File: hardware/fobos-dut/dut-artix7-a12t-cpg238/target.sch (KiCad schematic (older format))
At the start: 37 parts, among them J1 Target, J10 Barrel_Jack_Switch, J2 Pmod 2x6, U2 SP3003-04ATG, U3 SP3003-04ATG, U4 SP3003-04ATG, U7 TS3A5018DBQR

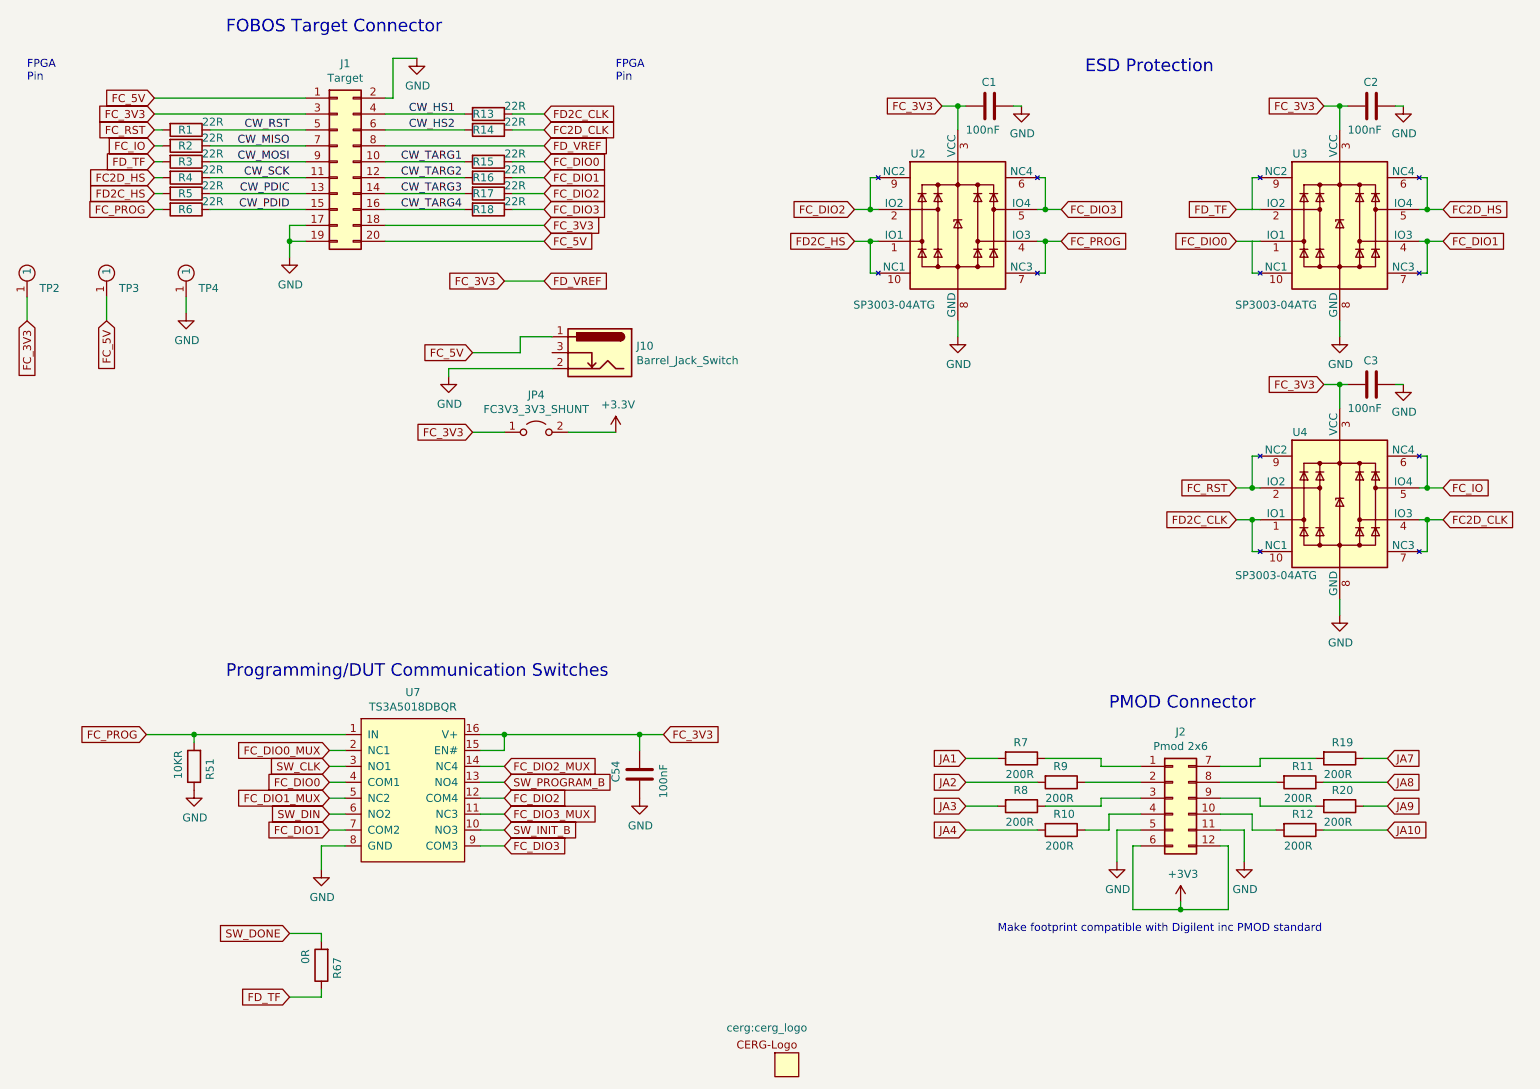
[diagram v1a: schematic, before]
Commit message: updated library ref for diode and FET, placed target connector and some parts
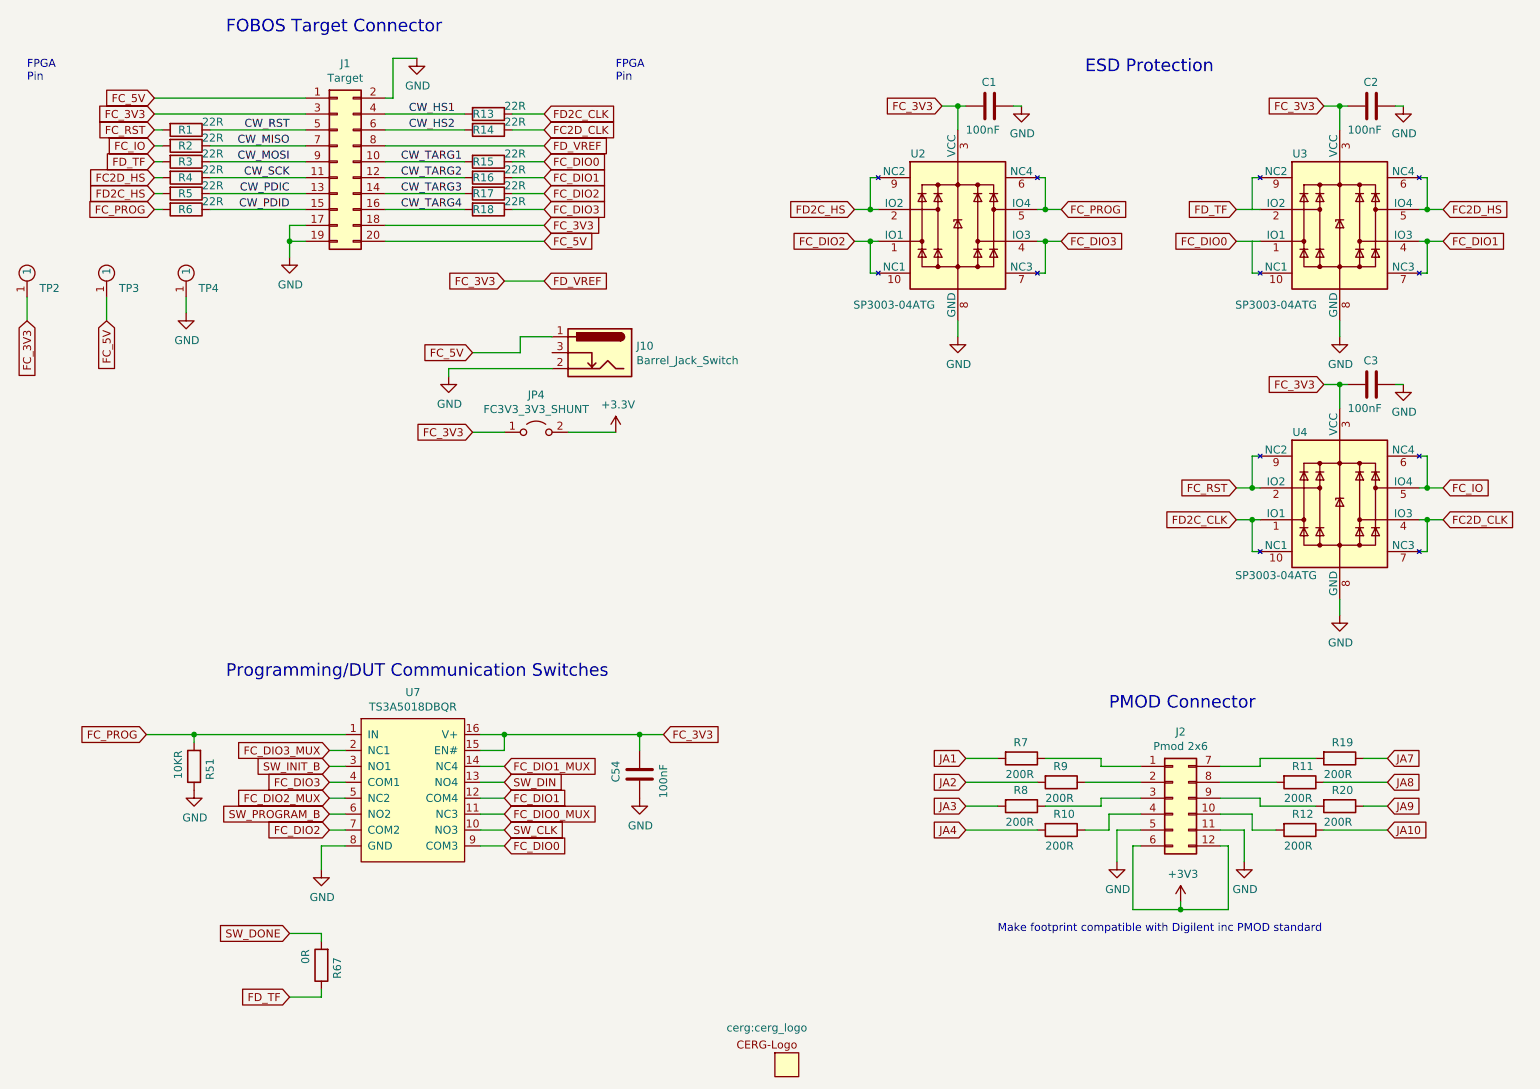
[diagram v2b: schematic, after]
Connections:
- net FC_DIO0: now also U7.9 (COM3); no longer U7.4 (COM1)
- net FC_DIO0_MUX: now also U7.11 (NC3); no longer U7.2 (NC1)
- net FC_DIO1: now also U7.12 (COM4); no longer U7.7 (COM2)
- net FC_DIO1_MUX: now also U7.14 (NC4); no longer U7.5 (NC2)
- net FC_DIO2: now also U2.1 (IO1), U2.10 (NC1), U7.7 (COM2); no longer U2.2 (IO2), U2.9 (NC2), U7.12 (COM4)
- net FC_DIO2_MUX: now also U7.5 (NC2); no longer U7.14 (NC4)
- net FC_DIO3: now also U2.4 (IO3), U2.7 (NC3), U7.4 (COM1); no longer U2.5 (IO4), U2.6 (NC4), U7.9 (COM3)
- net FC_DIO3_MUX: now also U7.2 (NC1); no longer U7.11 (NC3)
- net FC_PROG: now also U2.5 (IO4), U2.6 (NC4); no longer U2.4 (IO3), U2.7 (NC3)
- net FD2C_HS: now also U2.2 (IO2), U2.9 (NC2); no longer U2.1 (IO1), U2.10 (NC1)
- net SW_CLK: now also U7.10 (NO3); no longer U7.3 (NO1)
- net SW_DIN: now also U7.13 (NO4); no longer U7.6 (NO2)
- net SW_INIT_B: now also U7.3 (NO1); no longer U7.10 (NO3)
- net SW_PROGRAM_B: now also U7.6 (NO2); no longer U7.13 (NO4)
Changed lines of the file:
@@
 Wire Wire Line
 	4000 2400 4250 2400
-Text GLabel 7500 2150 2    50   Input ~ 0
+Text GLabel 7500 1950 2    50   Input ~ 0
 FC_PROG
 Text GLabel 8600 3900 0    50   Input ~ 0
 FD2C_CLK
-Text GLabel 6200 2150 0    50   Input ~ 0
+Text GLabel 6200 1950 0    50   Input ~ 0
 FD2C_HS
 Wire Wire Line
@@
 Wire Wire Line
 	6300 1950 6300 1750
-Text GLabel 7500 1950 2    50   Input ~ 0
+Text GLabel 7500 2150 2    50   Input ~ 0
 FC_DIO3
 Wire Wire Line
@@
 Text GLabel 6750 1300 0    50   Input ~ 0
 FC_3V3
-Text GLabel 6200 1950 0    50   Input ~ 0
+Text GLabel 6200 2150 0    50   Input ~ 0
 FC_DIO2
 $Comp
@@
 	1    0    0    -1
 $EndComp
+Text GLabel 4000 5850 2    50   Input ~ 0
+SW_CLK
+Text GLabel 4000 5750 2    50   Input ~ 0
+FC_DIO0_MUX
+Text GLabel 4000 5950 2    50   Input ~ 0
+FC_DIO0
+Text GLabel 4000 5550 2    50   Input ~ 0
+SW_DIN
+Text GLabel 4000 5450 2    50   Input ~ 0
+FC_DIO1_MUX
+Text GLabel 4000 5650 2    50   Input ~ 0
+FC_DIO1
+Text GLabel 2900 5550 0    50   Input ~ 0
+FC_DIO3
+Text GLabel 2900 5350 0    50   Input ~ 0
+FC_DIO3_MUX
 Text GLabel 2900 5450 0    50   Input ~ 0
-SW_CLK
-Text GLabel 2900 5350 0    50   Input ~ 0
-FC_DIO0_MUX
-Text GLabel 2900 5550 0    50   Input ~ 0
-FC_DIO0
+SW_INIT_B
+Text GLabel 2900 5850 0    50   Input ~ 0
+FC_DIO2
+Text GLabel 2900 5650 0    50   Input ~ 0
+FC_DIO2_MUX
 Text GLabel 2900 5750 0    50   Input ~ 0
-SW_DIN
-Text GLabel 2900 5650 0    50   Input ~ 0
-FC_DIO1_MUX
-Text GLabel 2900 5850 0    50   Input ~ 0
-FC_DIO1
-Text GLabel 4000 5950 2    50   Input ~ 0
-FC_DIO3
-Text GLabel 4000 5750 2    50   Input ~ 0
-FC_DIO3_MUX
-Text GLabel 4000 5850 2    50   Input ~ 0
-SW_INIT_B
-Text GLabel 4000 5650 2    50   Input ~ 0
-FC_DIO2
-Text GLabel 4000 5450 2    50   Input ~ 0
-FC_DIO2_MUX
-Text GLabel 4000 5550 2    50   Input ~ 0
 SW_PROGRAM_B
 Wire Wire Line

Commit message: fixed PMOD
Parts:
- J2: footprint Connector_PinHeader_2.54mm:PinHeader_2x06_P2.54mm_Horizontal -> fobos-shield:PinSocket_2x06_P2.54mm_Horizontal_FLipped
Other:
- note removed: "Make footprint compatible with Digilent inc PMOD standard"
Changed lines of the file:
@@
 F 0 "J2" H 8250 6067 50  0000 C CNN
 F 1 "Pmod 2x6" H 8250 5976 50  0000 C CNN
-F 2 "Connector_PinHeader_2.54mm:PinHeader_2x06_P2.54mm_Horizontal" H 8200 5650 50  0001 C CNN
+F 2 "fobos-shield:PinSocket_2x06_P2.54mm_Horizontal_FLipped" H 8200 5650 50  0001 C CNN
 F 3 "~" H 8200 5650 50  0001 C CNN
 F 4 "CONN HEADER R/A 12POS 2.54MM" H 8200 5650 50  0001 C CNN "Description"
@@
 	1    0    0    -1
 $EndComp
-Text Notes 7100 6500 0    50   ~ 0
-Make footprint compatible with Digilent inc PMOD standard
 $Comp
 L power:+3V3 #PWR?

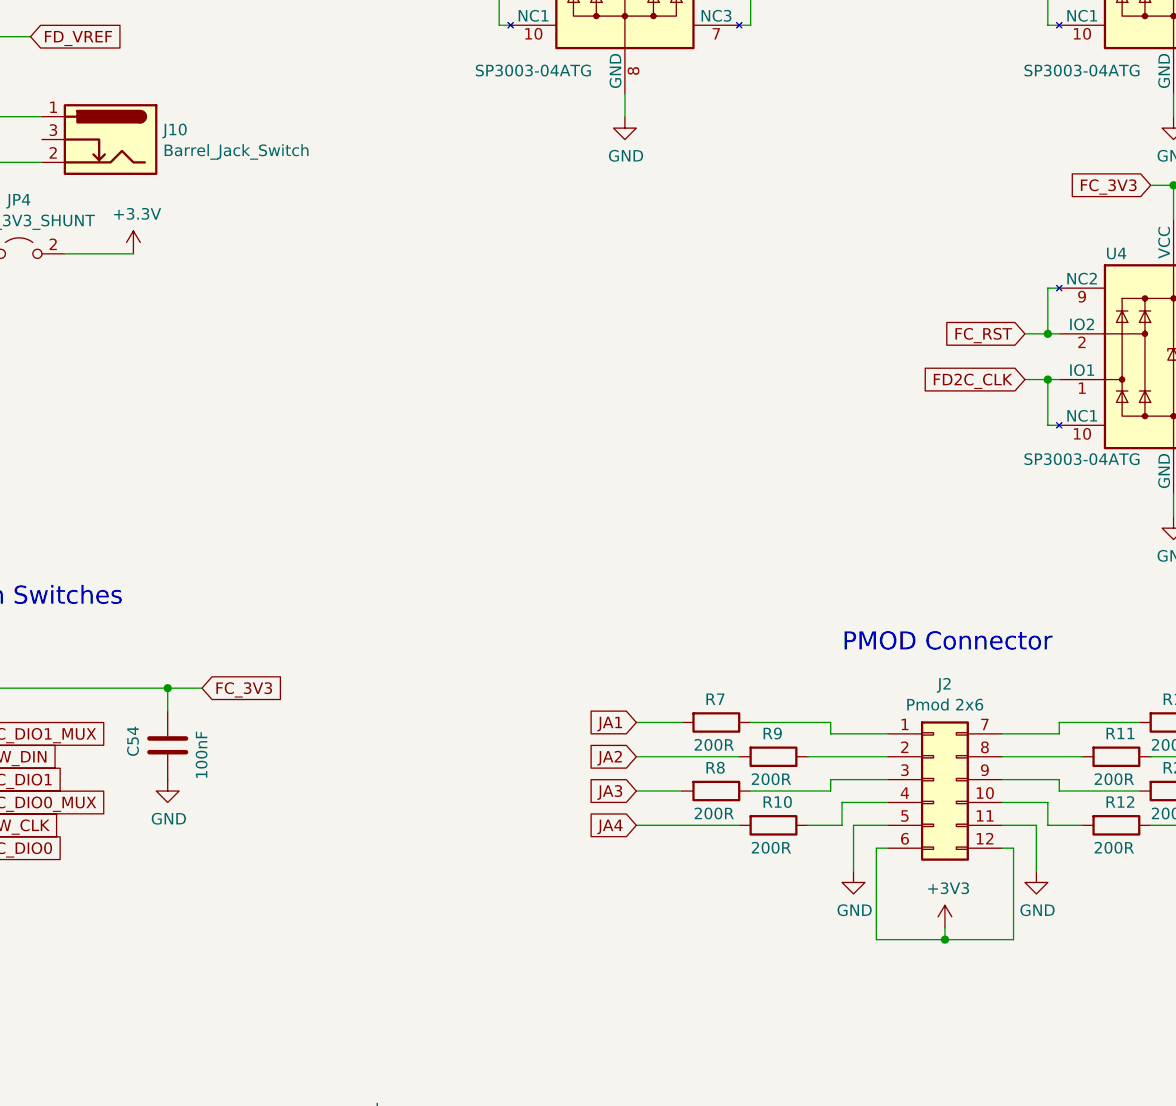
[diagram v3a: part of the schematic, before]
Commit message: added protection for PMOD
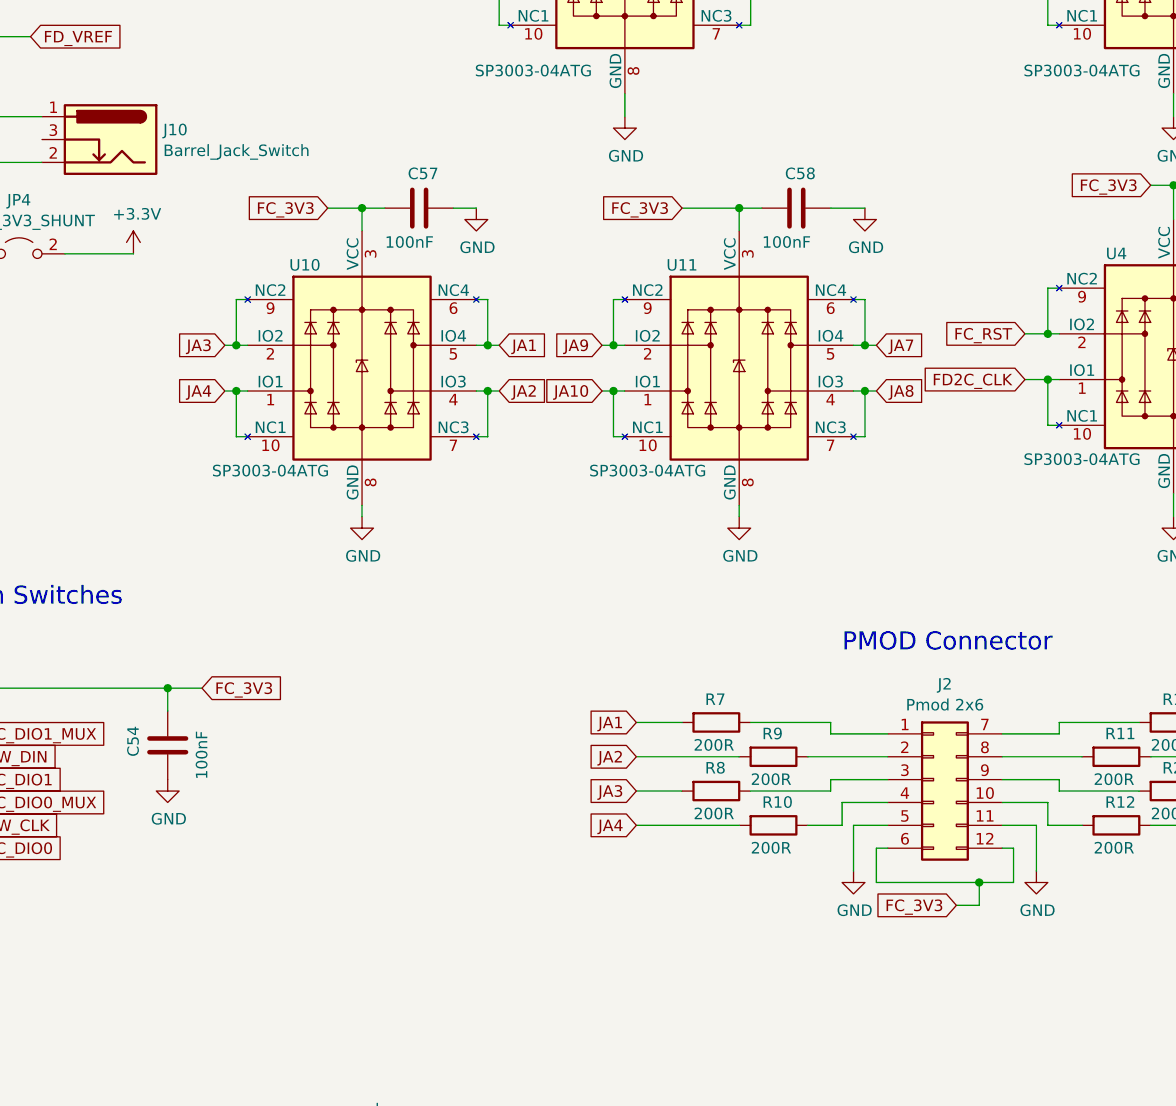
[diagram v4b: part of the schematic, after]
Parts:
- added C57, C58: 100nF, Capacitor_SMD:C_0603_1608Metric, symbol Device:C
- added U10, U11: SP3003-04ATG, Package_SO:MSOP-10_3x3mm_P0.5mm, symbol cerg:SP3003-04ATG
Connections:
- net +3V3: no longer J2.12 (Pin_12), J2.6 (Pin_6)
- net FC_3V3: now also J2.12 (Pin_12), J2.6 (Pin_6), C57.2, C58.2, U10.3 (VCC), U11.3 (VCC)
- net GND: now also C57.1, C58.1, U10.8 (GND), U11.8 (GND)
- net JA1: now also U10.5 (IO4), U10.6 (NC4)
- net JA10: now also U11.1 (IO1), U11.10 (NC1)
- net JA2: now also U10.4 (IO3), U10.7 (NC3)
- net JA3: now also U10.2 (IO2), U10.9 (NC2)
- net JA4: now also U10.1 (IO1), U10.10 (NC1)
- net JA7: now also U11.5 (IO4), U11.6 (NC4)
- net JA8: now also U11.4 (IO3), U11.7 (NC3)
- net JA9: now also U11.2 (IO2), U11.9 (NC2)

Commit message: everything placed on top except decoupling caps
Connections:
- net JA2: now also U10.2 (IO2), U10.9 (NC2); no longer U10.4 (IO3), U10.7 (NC3)
- net JA3: now also U11.5 (IO4), U11.6 (NC4); no longer U10.2 (IO2), U10.9 (NC2)
- net JA4: now also U11.2 (IO2), U11.9 (NC2); no longer U10.1 (IO1), U10.10 (NC1)
- net JA7: now also U10.4 (IO3), U10.7 (NC3); no longer U11.5 (IO4), U11.6 (NC4)
- net JA8: now also U10.1 (IO1), U10.10 (NC1); no longer U11.4 (IO3), U11.7 (NC3)
- net JA9: now also U11.4 (IO3), U11.7 (NC3); no longer U11.2 (IO2), U11.9 (NC2)
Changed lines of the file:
@@
 Text GLabel 6300 3750 2    50   Input ~ 0
 JA1
-Text GLabel 6300 3950 2    50   Input ~ 0
+Text GLabel 5100 3750 0    50   Input ~ 0
 JA2
-Text GLabel 5100 3750 0    50   Input ~ 0
+Text GLabel 7950 3750 2    50   Input ~ 0
 JA3
-Text GLabel 5100 3950 0    50   Input ~ 0
+Text GLabel 6750 3750 0    50   Input ~ 0
 JA4
 $Comp
@@
 	1    0    0    -1
 $EndComp
-Text GLabel 7950 3750 2    50   Input ~ 0
+Text GLabel 6300 3950 2    50   Input ~ 0
 JA7
+Text GLabel 5100 3950 0    50   Input ~ 0
+JA8
 Text GLabel 7950 3950 2    50   Input ~ 0
-JA8
-Text GLabel 6750 3750 0    50   Input ~ 0
 JA9
 Text GLabel 6750 3950 0    50   Input ~ 0

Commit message: almost last review
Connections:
- net FC_3V3: no longer U7.15 (EN#)
- net GND: now also U7.15 (EN#)
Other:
- moved on the sheet: C54
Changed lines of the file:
@@
 Comment1 "License: Apache License Version 2.0"
 Comment2 "Copyright © Cryptographic Engineering Research Group"
-Comment3 "Author: Jens-Peter Kaps"
+Comment3 "Author: Jens-Peter Kaps, Eddie Ferrufino"
 Comment4 "Project: FOBOS Artix-7 a12t DUT"
 $EndDescr
@@
 L Device:C C?
 U 1 1 6025643D
-P 4850 5500
+P 5300 5500
 AR Path="/5F227C5D/6025643D" Ref="C?"  Part="1"
 AR Path="/5F20DA36/6025643D" Ref="C54"  Part="1"
-F 0 "C54" V 4700 5450 50  0000 L CNN
-F 1 "100nF" V 5000 5350 50  0000 L CNN
-F 2 "Capacitor_SMD:C_0603_1608Metric" H 4888 5350 50  0001 C CNN
-F 3 "~" H 4850 5500 50  0001 C CNN
-F 4 "CAP CER 0.1UF 6.3V X7R 0603" H 4850 5500 50  0001 C CNN "Description"
-F 5 "06036C104KAT4A" H 4850 5500 50  0001 C CNN "MPN"
-F 6 "AVX Corporation" H 4850 5500 50  0001 C CNN "Manufacturer"
-	1    4850 5500
+F 0 "C54" V 5150 5450 50  0000 L CNN
+F 1 "100nF" V 5450 5350 50  0000 L CNN
+F 2 "Capacitor_SMD:C_0603_1608Metric" H 5338 5350 50  0001 C CNN
+F 3 "~" H 5300 5500 50  0001 C CNN
+F 4 "CAP CER 0.1UF 6.3V X7R 0603" H 5300 5500 50  0001 C CNN "Description"
+F 5 "06036C104KAT4A" H 5300 5500 50  0001 C CNN "MPN"
+F 6 "AVX Corporation" H 5300 5500 50  0001 C CNN "Manufacturer"
+	1    5300 5500
 	1    0    0    -1
 $EndComp
-Text GLabel 5000 5250 2    50   Input ~ 0
+Text GLabel 5450 5250 2    50   Input ~ 0
 FC_3V3
 Wire Wire Line
-	4850 5350 4850 5250
-Connection ~ 4850 5250
+	5300 5350 5300 5250
+Connection ~ 5300 5250
 Wire Wire Line
-	4850 5250 5000 5250
+	5300 5250 5450 5250
 $Comp
 L power:GND #PWR?
 U 1 1 602946AE
-P 4850 5650
+P 5300 5650
 AR Path="/5B6C87CC/602946AE" Ref="#PWR?"  Part="1"
 AR Path="/5B5AB131/602946AE" Ref="#PWR?"  Part="1"
@@
 AR Path="/5F227C5D/602946AE" Ref="#PWR?"  Part="1"
 AR Path="/5F20DA36/602946AE" Ref="#PWR041"  Part="1"
-F 0 "#PWR041" H 4850 5400 50  0001 C CNN
-F 1 "GND" H 4855 5477 50  0000 C CNN
-F 2 "" H 4850 5650 50  0001 C CNN
-F 3 "" H 4850 5650 50  0001 C CNN
-	1    4850 5650
+F 0 "#PWR041" H 5300 5400 50  0001 C CNN
+F 1 "GND" H 5305 5477 50  0000 C CNN
+F 2 "" H 5300 5650 50  0001 C CNN
+F 3 "" H 5300 5650 50  0001 C CNN
+	1    5300 5650
 	1    0    0    -1
 $EndComp
@@
 Wire Wire Line
 	4000 5950 3850 5950
-Wire Wire Line
-	3850 5250 4000 5250
-Wire Wire Line
-	3850 5350 4000 5350
-Wire Wire Line
-	4000 5350 4000 5250
-Connection ~ 4000 5250
-Wire Wire Line
-	4000 5250 4850 5250
 Text GLabel 2650 6500 0    50   Input ~ 0
 SW_DONE
@@
 Text GLabel 4250 1350 2    50   Input ~ 0
 FD2C_CLK
+Wire Wire Line
+	3850 5250 5300 5250
+$Comp
+L power:GND #PWR?
+U 1 1 6221A5F4
+P 5000 5650
+AR Path="/5B6C87CC/6221A5F4" Ref="#PWR?"  Part="1"
+AR Path="/5B5AB131/6221A5F4" Ref="#PWR?"  Part="1"
+AR Path="/5BE3725D/6221A5F4" Ref="#PWR?"  Part="1"
+AR Path="/5F227C5D/6221A5F4" Ref="#PWR?"  Part="1"
+AR Path="/5F20DA36/6221A5F4" Ref="#PWR0115"  Part="1"
+F 0 "#PWR0115" H 5000 5400 50  0001 C CNN
+F 1 "GND" H 5005 5477 50  0000 C CNN
+F 2 "" H 5000 5650 50  0001 C CNN
+F 3 "" H 5000 5650 50  0001 C CNN
+	1    5000 5650
+	1    0    0    -1
+$EndComp
+Wire Wire Line
+	3850 5350 5000 5350
+Wire Wire Line
+	5000 5350 5000 5650
 $EndSCHEMATC
